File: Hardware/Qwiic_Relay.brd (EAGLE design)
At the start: 25.4 x 55.9 mm, 50 parts, among them J2 Qwiic Right Angle, J3 Qwiic Right Angle, J4 AVR_SPI_PROG_3X2TESTPOINTS, Q4 600mA/40V, U1 ATTIN85_SOIC_5.3MM, U2 OPTO_ISOLATOR

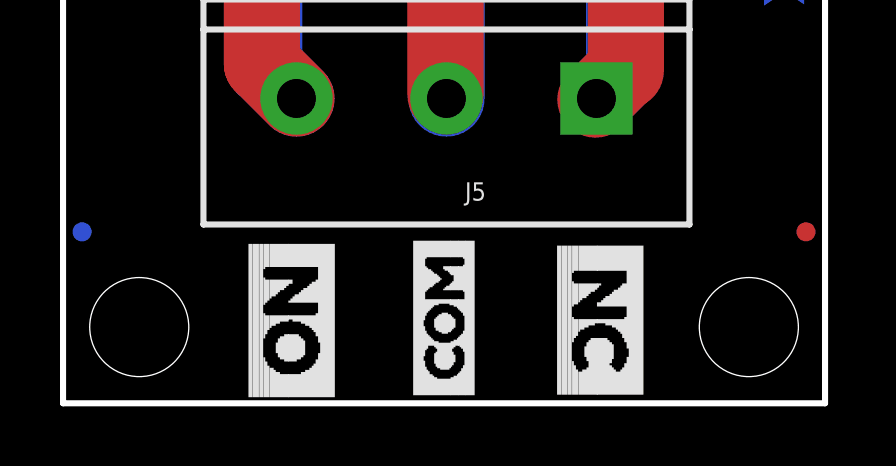
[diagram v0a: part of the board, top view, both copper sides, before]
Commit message: fixed buzzard label
fixed the flipped labels NC and NO. now they match the direction of COM and what the rest of the text orientations
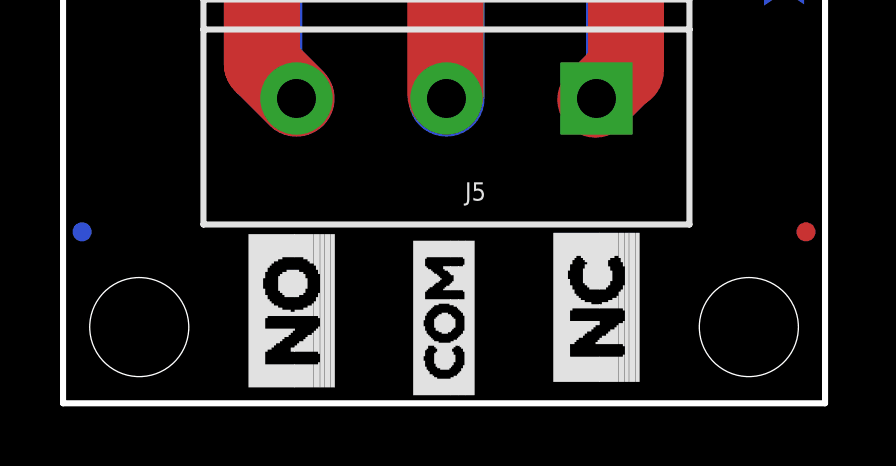
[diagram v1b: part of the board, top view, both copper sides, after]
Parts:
- moved U$11 6.60 mm to (7.62, -5.46), turned to 90 degrees
- moved U$20 6.22 mm to (17.8, -5.21), turned to 90 degrees

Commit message: Small changes to silk and version number
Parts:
- moved LOGO1 1.02 mm to (2.41, 6.35), turned to 270 degrees
- moved U$10 0.28 mm to (19.6, 32.3)
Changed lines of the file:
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@@
 <?xml version="1.0" encoding="utf-8"?>
 <!DOCTYPE eagle SYSTEM "eagle.dtd">
-<eagle version="7.7.0">
+<eagle version="9.0.0">
 <drawing>
 <settings>
 <setting alwaysvectorfont="yes"/>
+<setting keepoldvectorfont="yes"/>
 <setting verticaltext="up"/>
 </settings>
@@
 <layer number="17" name="Pads" color="2" fill="1" visible="yes" active="yes"/>
 <layer number="18" name="Vias" color="2" fill="1" visible="yes" active="yes"/>
-<layer number="19" name="Unrouted" color="6" fill="1" visible="yes" active="yes"/>
+<layer number="19" name="Unrouted" color="6" fill="1" visible="no" active="yes"/>
 <layer number="20" name="Dimension" color="15" fill="1" visible="yes" active="yes"/>
 <layer number="21" name="tPlace" color="16" fill="1" visible="yes" active="yes"/>
@@
 <layer number="44" name="Drills" color="7" fill="1" visible="no" active="yes"/>
 <layer number="45" name="Holes" color="7" fill="1" visible="yes" active="yes"/>
-<layer number="46" name="Milling" color="3" fill="1" visible="no" active="yes"/>
+<layer number="46" name="Milling" color="3" fill="1" visible="yes" active="yes"/>
 <layer number="47" name="Measures" color="7" fill="1" visible="no" active="yes"/>
 <layer number="48" name="Document" color="7" fill="1" visible="no" active="yes"/>
 <layer number="49" name="Reference" color="7" fill="1" visible="no" active="yes"/>
 <layer number="50" name="dxf" color="7" fill="1" visible="no" active="yes"/>
-<layer number="51" name="tDocu" color="6" fill="1" visible="yes" active="yes"/>
+<layer number="51" name="tDocu" color="6" fill="1" visible="no" active="yes"/>
 <layer number="52" name="bDocu" color="7" fill="1" visible="no" active="yes"/>
 <layer number="91" name="Nets" color="2" fill="1" visible="no" active="no"/>
@@
 1 Oz Cu</text>
 <circle x="10.16" y="44.45" radius="0.1778" width="0.1778" layer="22"/>
-<text x="24.257" y="10.16" size="1.778" layer="16" ratio="15" rot="MR90" align="center">x12</text>
+<text x="22.86" y="8.89" size="1.778" layer="16" ratio="15" rot="SMR270" align="center">x12</text>
 <dimension x1="25.4" y1="50.8" x2="0" y2="50.8" x3="12.7" y3="58.42" textsize="1.778" textratio="15" layer="47" unit="inch"/>
 <dimension x1="25.4" y1="50.8" x2="25.4" y2="0" x3="39.37" y3="25.4" textsize="1.778" textratio="15" layer="47" unit="inch" visible="yes"/>
@@
 <wire x1="15.24" y1="32.512" x2="10.16" y2="32.512" width="0.1778" layer="41"/>
 <dimension x1="12.7" y1="30.099" x2="12.7" y2="32.893" x3="11.43" y3="31.496" textsize="0.2032" textratio="15" layer="47" dtype="vertical" width="0.0254" visible="yes"/>
-<dimension x1="13.843" y1="29.591" x2="16.51" y2="32.004" x3="15.302865625" y3="30.65783125" textsize="0.2032" textratio="15" layer="47" width="0.0254" visible="yes"/>
+<dimension x1="13.843" y1="29.591" x2="16.51" y2="32.004" x3="15.3028625" y3="30.65783125" textsize="0.2032" textratio="15" layer="47" width="0.0254" visible="yes"/>
 <dimension x1="11.684" y1="29.591" x2="9.017" y2="32.131" x3="10.099821875" y3="30.5977875" textsize="0.2032" textratio="15" layer="47" width="0.0254" visible="yes"/>
 <text x="9.779" y="23.876" size="0.508" layer="46" font="vector" ratio="15" rot="R90">route out</text>
@@
 <param name="dpMaxLengthDifference" value="10mm"/>
 <param name="dpGapFactor" value="2.5"/>
-<param name="checkGrid" value="0"/>
 <param name="checkAngle" value="1"/>
 <param name="checkFont" value="1"/>
 <param name="checkRestrict" value="1"/>
+<param name="checkStop" value="0"/>
+<param name="checkValues" value="0"/>
 <param name="useDiameter" value="13"/>
 <param name="maxErrors" value="50"/>
@@
 </element>
 <element name="U$3" library="SparkX" package="SPARKX-MEDIUM" value="SPARKX-LOGO4" x="2.159" y="20.32" rot="R90"/>
-<element name="LOGO1" library="SparkFun-Aesthetics" package="OSHW-LOGO-MINI" value="OSHW-LOGOMINI" x="1.397" y="6.35" rot="MR90"/>
+<element name="LOGO1" library="SparkFun-Aesthetics" package="OSHW-LOGO-MINI" value="OSHW-LOGOMINI" x="2.413" y="6.35" rot="MR270"/>
 <element name="U$4" library="SparkX" package="SPARKX-MEDIUM" value="SPARKX-LOGO4" x="2.159" y="20.32" rot="MR270"/>
 <element name="JP3" library="SparkFun" package="STAND-OFF" value="STAND-OFF" x="2.54" y="48.26"/>
@@
 <element name="U$7" library="Labels-0_04" package="3.3V" value="" x="11.43" y="49.022" rot="MR270"/>
 <element name="U$8" library="Labels-0_04" package="GND" value="" x="8.89" y="49.022" rot="MR270"/>
-<element name="U$10" library="buzzard_labels" package="ACT5" value="" x="19.685" y="32.512" rot="R90"/>
+<element name="U$10" library="buzzard_labels" package="ACT5" value="" x="19.558" y="32.258" rot="R90"/>
 <element name="U$15" library="buzzard_labels" package="QWIIC_RELAY1" value="" x="22.86" y="13.589" rot="R90"/>
 <element name="U$16" library="buzzard_labels" package="QWIIC_RELAY1" value="" x="22.86" y="28.321" rot="MR270"/>
@@
 <element name="U$20" library="buzzard_labels" package="NC3" value="" x="17.78" y="-5.207" rot="R90"/>
 <element name="J5" library="SparkFun-Connectors" package="SCREWTERMINAL-5MM-3" value="" x="17.78" y="5.08" rot="R180">
+<attribute name="PROD_ID" value="CONN-10134" x="17.78" y="5.08" size="1.778" layer="27" font="vector" ratio="15" rot="R180" display="off"/>
 <attribute name="SF_SKU" value="PRT-08433" x="17.78" y="5.08" size="1.778" layer="27" font="vector" ratio="15" rot="R180" display="off"/>
-<attribute name="PROD_ID" value="CONN-10134" x="17.78" y="5.08" size="1.778" layer="27" font="vector" ratio="15" rot="R180" display="off"/>
 </element>
 </elements>

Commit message: Adding Qwiic Logo to bottom silk
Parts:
- added U$1: (no value), Labels:QWIIC-LOGO-MEDIUM
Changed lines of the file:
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@@
 <layer number="59" name="tCarbon" color="7" fill="1" visible="no" active="no"/>
 <layer number="60" name="bCarbon" color="7" fill="1" visible="no" active="no"/>
+<layer number="88" name="SimResults" color="7" fill="1" visible="no" active="no"/>
+<layer number="89" name="SimProbes" color="7" fill="1" visible="no" active="no"/>
 <layer number="90" name="Modules" color="5" fill="1" visible="no" active="no"/>
 <layer number="97" name="Info" color="7" fill="1" visible="no" active="no"/>
@@
 1 Oz Cu</text>
 <circle x="10.16" y="44.45" radius="0.1778" width="0.1778" layer="22"/>
-<text x="22.86" y="8.89" size="1.778" layer="16" ratio="15" rot="SMR270" align="center">x12</text>
+<text x="22.86" y="3.81" size="1.778" layer="16" ratio="15" rot="SMR270" align="center">x12</text>
 <dimension x1="25.4" y1="50.8" x2="0" y2="50.8" x3="12.7" y3="58.42" textsize="1.778" textratio="15" layer="47" unit="inch"/>
 <dimension x1="25.4" y1="50.8" x2="25.4" y2="0" x3="39.37" y3="25.4" textsize="1.778" textratio="15" layer="47" unit="inch" visible="yes"/>
@@
 <attribute name="SF_SKU" value="PRT-08433" x="17.78" y="5.08" size="1.778" layer="27" font="vector" ratio="15" rot="R180" display="off"/>
 </element>
+<element name="U$1" library="Labels" package="QWIIC-LOGO-MEDIUM" value="" x="21.59" y="10.16" rot="MR270"/>
 </elements>
 <signals>
